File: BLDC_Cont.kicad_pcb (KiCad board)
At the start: 4 copper layers, 31.1 x 21.6 mm, 24 parts, among them J1 Conn, J2 Conn, J3 Conn, J4 Conn_01x05_Female, J5 Conn_01x02_Female, Q1 BUK9Y14-80E, Q2 BUK9Y14-80E, U1 ADUM7234

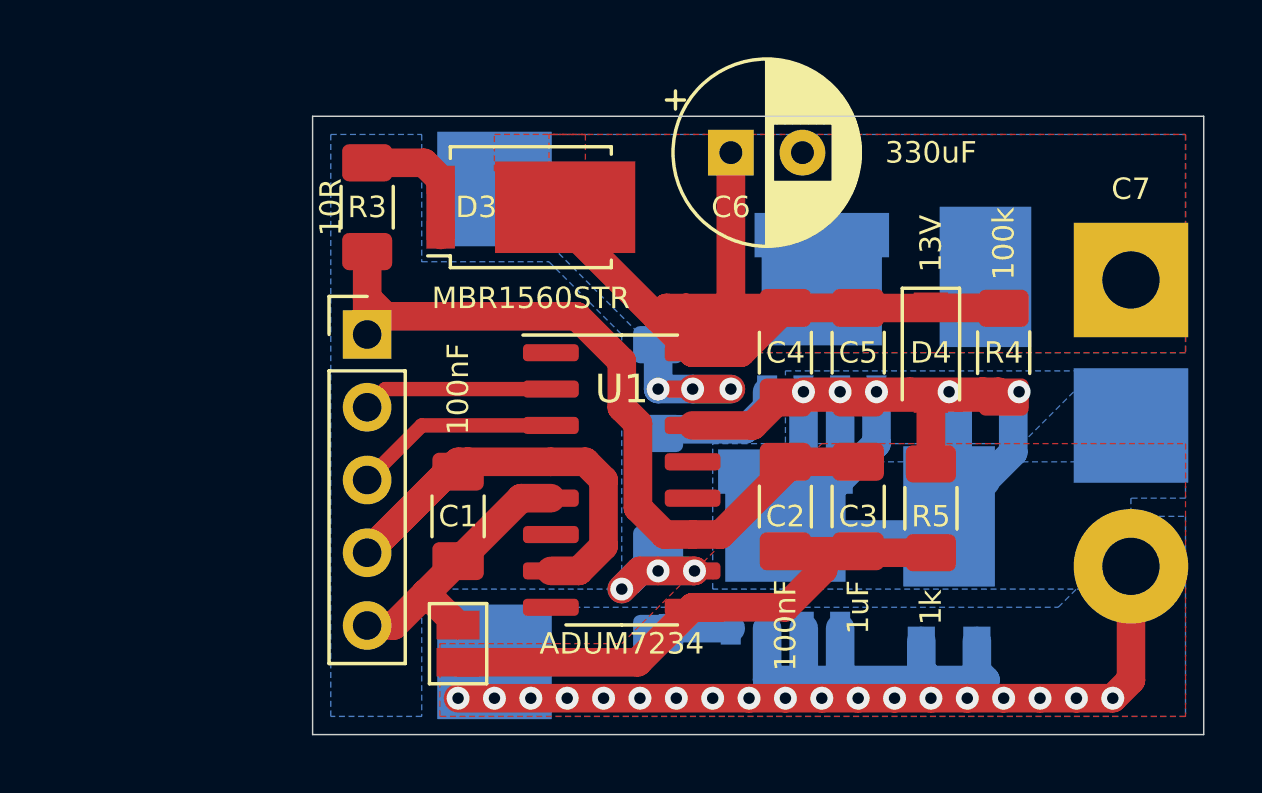
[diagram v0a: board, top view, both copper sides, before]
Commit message: Rev. 3
Updated Revision (3)
-Organized files
-Removed legacy documentation
-Found cross-conduction protection of ADuM7234 was **NOT** satisfactory.
+Added NOR gate based mutual exclusion circuit.
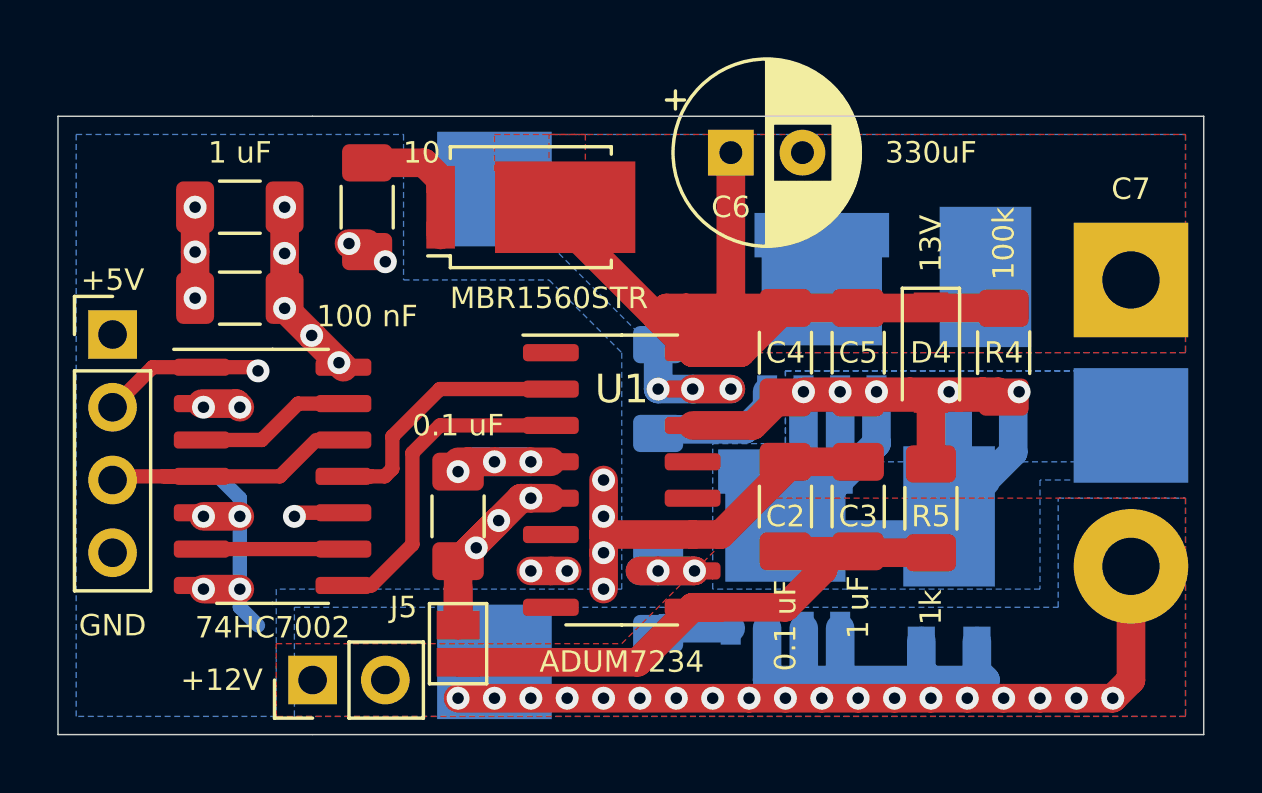
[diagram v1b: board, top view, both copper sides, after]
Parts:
- added C8: 1 uF, Capacitor_SMD:C_1206_3216Metric_Pad1.33x1.80mm_HandSolder, F.Cu at (156.8, 108.0)
- added C9: 100 nF, Capacitor_SMD:C_1206_3216Metric_Pad1.33x1.80mm_HandSolder, F.Cu at (156.8, 111.1)
- added J6: Pin Headder, Connector_PinHeader_2.54mm:PinHeader_1x02_P2.54mm_Vertical, F.Cu at (159.4, 124.5)
- added U2: 74HC7002, Package_SO:SOIC-14_3.9x8.7mm_P1.27mm, F.Cu at (158.0, 117.3)
- C1, C2: value 100nF -> 0.1 uF
- C3: value 1uF -> 1 uF
- J4: value Conn_01x05_Female -> Pin Headder; footprint Connector_PinHeader_2.54mm:PinHeader_1x05_P2.54mm_Vertical -> Connector_PinHeader_2.54mm:PinHeader_1x04_P2.54mm_Vertical
- J5: value Conn_01x02_Female -> GND_Jumper
- R2, R3: value 10R -> 10
- moved J4 8.89 mm to (152.4, 112.4)
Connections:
- net GND renamed GNDPWR
- J4 pad 1: +12V -> +5VD
- J4 pad 4: +5VD -> GNDD
- U1 pad 2: /PWM_A -> /A_Safe
- U1 pad 3: /PWM_B -> /B_Safe
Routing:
- net GNDPWR: track 65.9 -> 88.8 mm
- net +12V: track 27.3 -> 45.0 mm, vias 0 -> 6
- net GNDD: track 9.84 -> 22.4 mm, vias 0 -> 12
- net /B_Safe: track 0.00 -> 12.4 mm
- net +5VD: track 19.2 -> 29.5 mm, vias 0 -> 10
- net /A_Safe: track 0.00 -> 9.16 mm
- net /PWM_A: track 6.68 -> 13.1 mm, vias 0 -> 2
- net /nA: track 0.00 -> 4.56 mm
- net /nB: track 0.00 -> 4.03 mm
- net /V_OL: track 7.30 -> 5.07 mm, vias 3 -> 2
- net /PWM_B: track 7.20 -> 9.03 mm
- added copper zone on In2.Cu, net +5VD
- removed copper zone on In2.Cu, net GNDPWR
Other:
- board size 31.1 x 21.6 mm -> 40 x 21.6 mm
